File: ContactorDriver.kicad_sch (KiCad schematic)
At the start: 25 parts, among them J1 PowerConn, J2 DashboardConn, J3 ContactorConn, J4 FanConn1, J5 FanConn2, Q1 CSD18511KTT, Q3 CSD18511KTT, U1 RI3-1212S

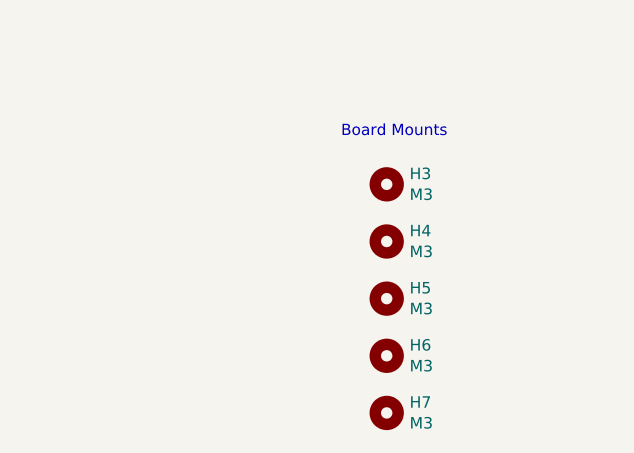
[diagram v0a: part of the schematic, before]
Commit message: Layout completed
Layout attempts to mirror connections on the original V2.1 CDB but in a drastically smaller package.
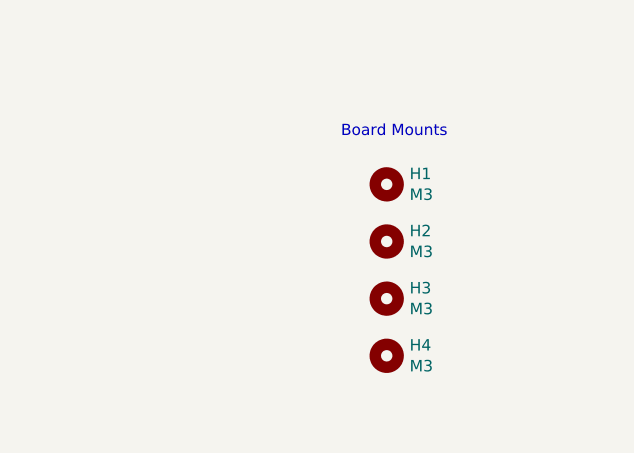
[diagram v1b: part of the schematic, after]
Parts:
- removed H7: M3, MountingHole:MountingHole_3mm, symbol Mechanical:MountingHole
- renumbered H3 to H1, H4 to H2, H5 to H3, H6 to H4
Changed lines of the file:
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@@
 		(on_board yes)
 		(dnp no)
-		(property "Reference" "H3"
+		(property "Reference" "H1"
 			(at 278.13 135.3566 0)
 			(effects
@@
 			(project "ContactorDriver"
 				(path "/aaa5c8ef-bb12-4c4a-bd2b-ddbca3d09ae8"
-					(reference "H3")
+					(reference "H1")
 					(unit 1)
 				)
@@
 		(on_board yes)
 		(dnp no)
-		(property "Reference" "H4"
+		(property "Reference" "H2"
 			(at 278.13 141.7066 0)
 			(effects
@@
 			(project "ContactorDriver"
 				(path "/aaa5c8ef-bb12-4c4a-bd2b-ddbca3d09ae8"
-					(reference "H4")
+					(reference "H2")
 					(unit 1)
 				)
@@
 		(on_board yes)
 		(dnp no)
-		(property "Reference" "H5"
+		(property "Reference" "H3"
 			(at 278.13 148.0566 0)
 			(effects
@@
 			(project "ContactorDriver"
 				(path "/aaa5c8ef-bb12-4c4a-bd2b-ddbca3d09ae8"
-					(reference "H5")
+					(reference "H3")
 					(unit 1)
 				)
@@
 		(on_board yes)
 		(dnp no)
-		(property "Reference" "H6"
+		(property "Reference" "H4"
 			(at 278.13 154.4066 0)
 			(effects
@@
 			(project "ContactorDriver"
 				(path "/aaa5c8ef-bb12-4c4a-bd2b-ddbca3d09ae8"
-					(reference "H6")
+					(reference "H4")
 					(unit 1)
 				)
@@
 					(unit 1)
 				)
-			)
-		)
-	)
-	(symbol
-		(lib_id "Mechanical:MountingHole")
-		(at 275.59 161.925 0)
-		(unit 1)
-		(exclude_from_sim no)
-		(in_bom yes)
-		(on_board yes)
-		(dnp no)
-		(property "Reference" "H7"
-			(at 278.13 160.7566 0)
-			(effects
-				(font
-					(size 1.27 1.27)
-				)
-				(justify left)
-			)
-		)
-		(property "Value" "M3"
-			(at 278.13 163.068 0)
-			(effects
-				(font
-					(size 1.27 1.27)
-				)
-				(justify left)
-			)
-		)
-		(property "Footprint" "MountingHole:MountingHole_3mm"
-			(at 275.59 161.925 0)
-			(effects
-				(font
-					(size 1.27 1.27)
-				)
-				(hide yes)
-			)
-		)
-		(property "Datasheet" "~"
-			(at 275.59 161.925 0)
-			(effects
-				(font
-					(size 1.27 1.27)
-				)
-				(hide yes)
-			)
-		)
-		(property "Description" ""
-			(at 275.59 161.925 0)
-			(effects
-				(font
-					(size 1.27 1.27)
-				)
-				(hide yes)
-			)
-		)
-		(instances
-			(project "ContactorDriver"
-				(path "/aaa5c8ef-bb12-4c4a-bd2b-ddbca3d09ae8"
-					(reference "H7")
-					(unit 1)
-				)

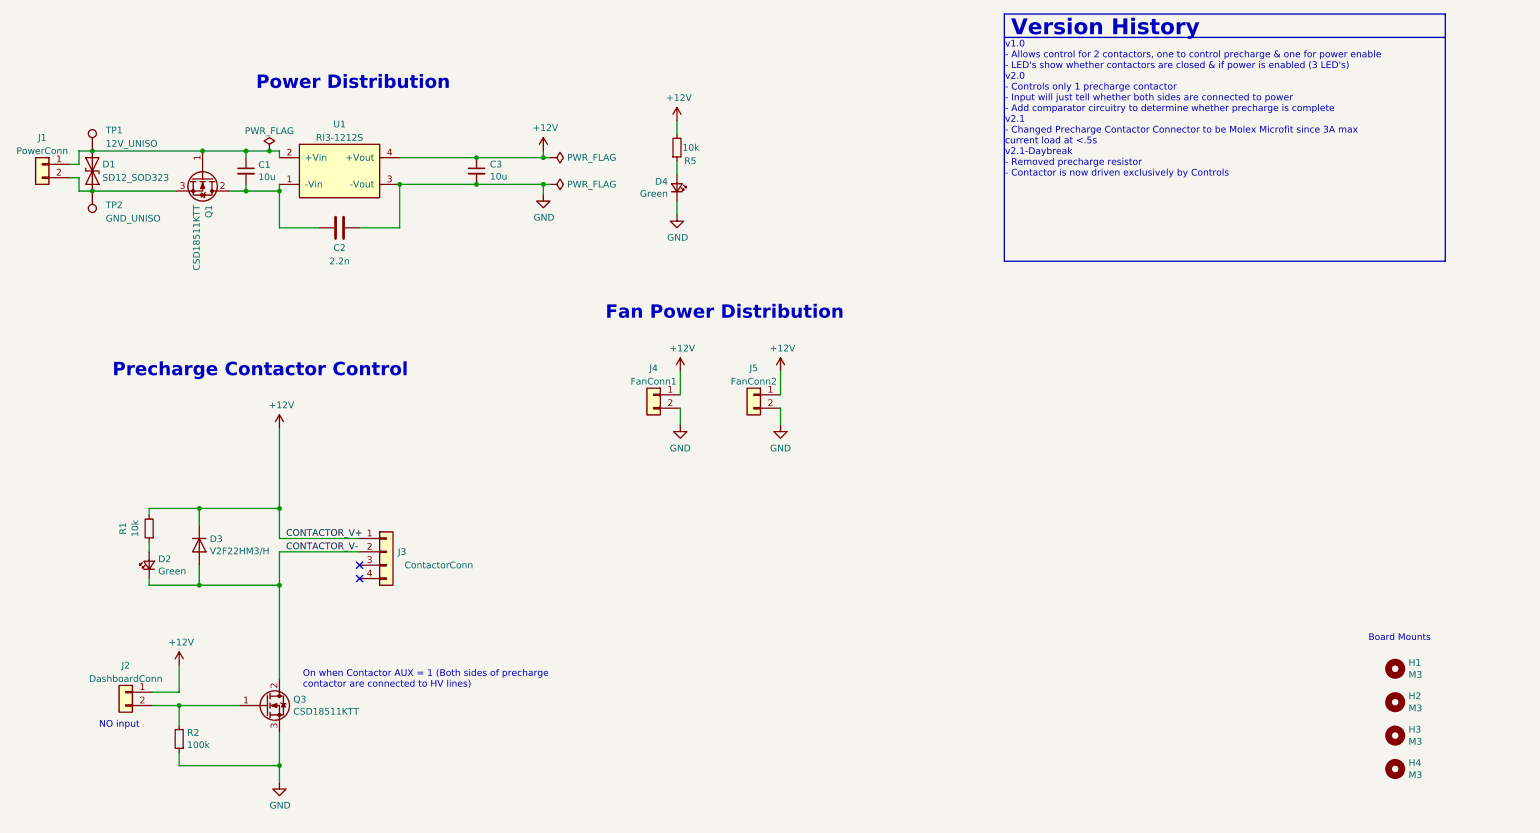
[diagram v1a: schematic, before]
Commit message: Updated Schematic
Updated Schematic to include ability to drive 2 contactors separately, and fans are now controlled by contactor signal as well.
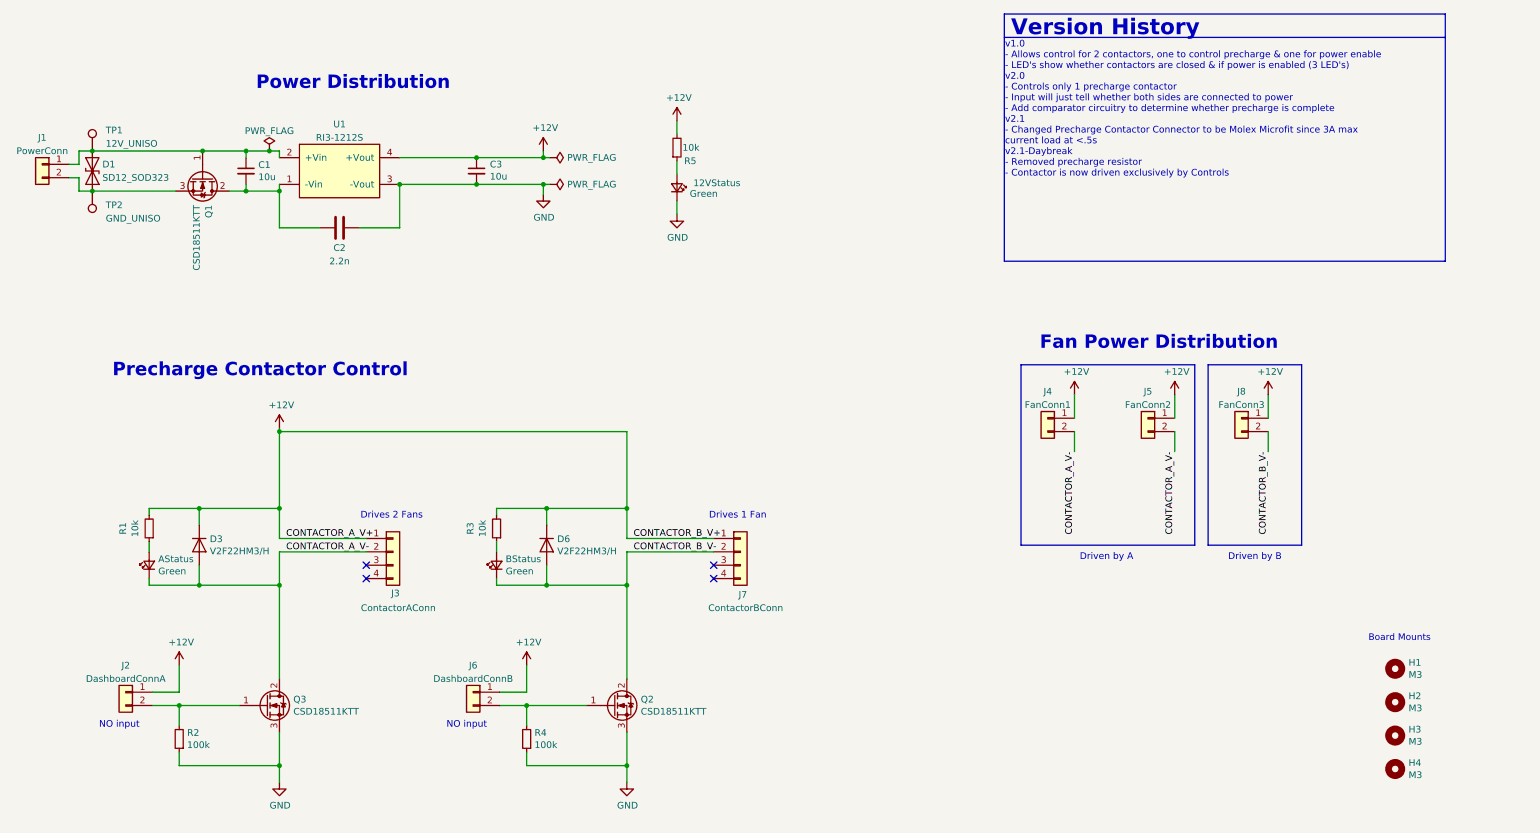
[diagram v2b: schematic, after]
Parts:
- added BStatus: Green, LED_SMD:LED_0805_2012Metric_Pad1.15x1.40mm_HandSolder, symbol Device:LED_Small
- added D6: V2F22HM3/H, UTSVT_Passive:V2F22HM, symbol Device:D
- added J6: DashboardConnB, Connector_Molex:Molex_Micro-Fit_3.0_43650-0200_1x02_P3.00mm_Horizontal, symbol Connector_Generic:Conn_01x02
- added J7: ContactorBConn, UTSVT_Connectors:Molex_MicroFit3.0_1x4xP3.00mm_PolarizingPeg_Vertical, symbol Connector_Generic:Conn_01x04
- added J8: FanConn3, Connector_Molex:Molex_Micro-Fit_3.0_43650-0200_1x02_P3.00mm_Horizontal, symbol Connector_Generic:Conn_01x02
- added Q2: CSD18511KTT, Package_TO_SOT_SMD:TO-252-2, symbol Device:Q_NMOS_GDS
- added R3: 10k, Resistor_SMD:R_0805_2012Metric, symbol Device:R_Small
- added R4: 100k, Resistor_SMD:R_0805_2012Metric_Pad1.20x1.40mm_HandSolder, symbol Device:R_Small
- J2: value DashboardConn -> DashboardConnA
- J3: value ContactorConn -> ContactorAConn
- renumbered D4 to 12VStatus, D2 to AStatus
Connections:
- net +12V: now also D6.1 (K), J6.1 (Pin_1), J7.1 (Pin_1), J8.1 (Pin_1), R3.2
- net GND: now also Q2.3 (S), R4.1; no longer J4.2 (Pin_2), J5.2 (Pin_2)
- net CONTACTOR_V- renamed CONTACTOR_A_V-
- net CONTACTOR_A_V-: now also J4.2 (Pin_2), J5.2 (Pin_2)
- new net: J6.2 (Pin_2), Q2.1 (G), R4.2
- new net: BStatus.2 (A), R3.1
- new net CONTACTOR_B_V-: BStatus.1 (K), D6.2 (A), J7.2 (Pin_2), J8.2 (Pin_2), Q2.2 (D)
- no-connect marks 2 -> 4
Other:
- note added: "Driven by A"
- note added: "Driven by B"
- note added: "Drives 1 Fan"
- note added: "Drives 2 Fans"
- note removed: "On when Contactor AUX = 1 (Both sides of precharge contactor are connected to HV lines)"
- moved on the sheet: J3, J4, J5

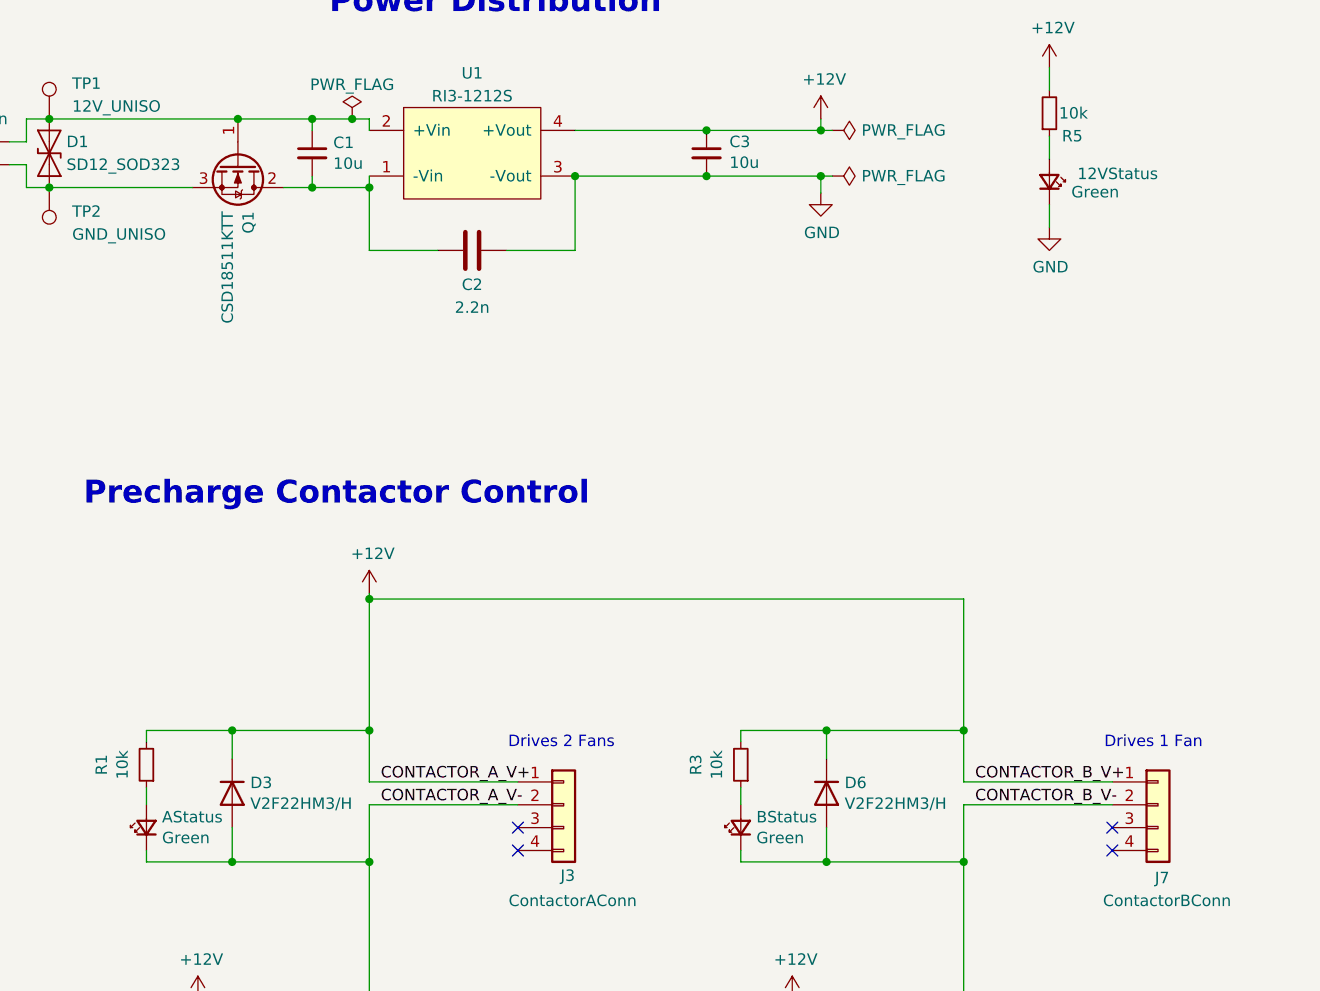
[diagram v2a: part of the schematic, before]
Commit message: Layout Updated
Updated layout to match updated schematic.
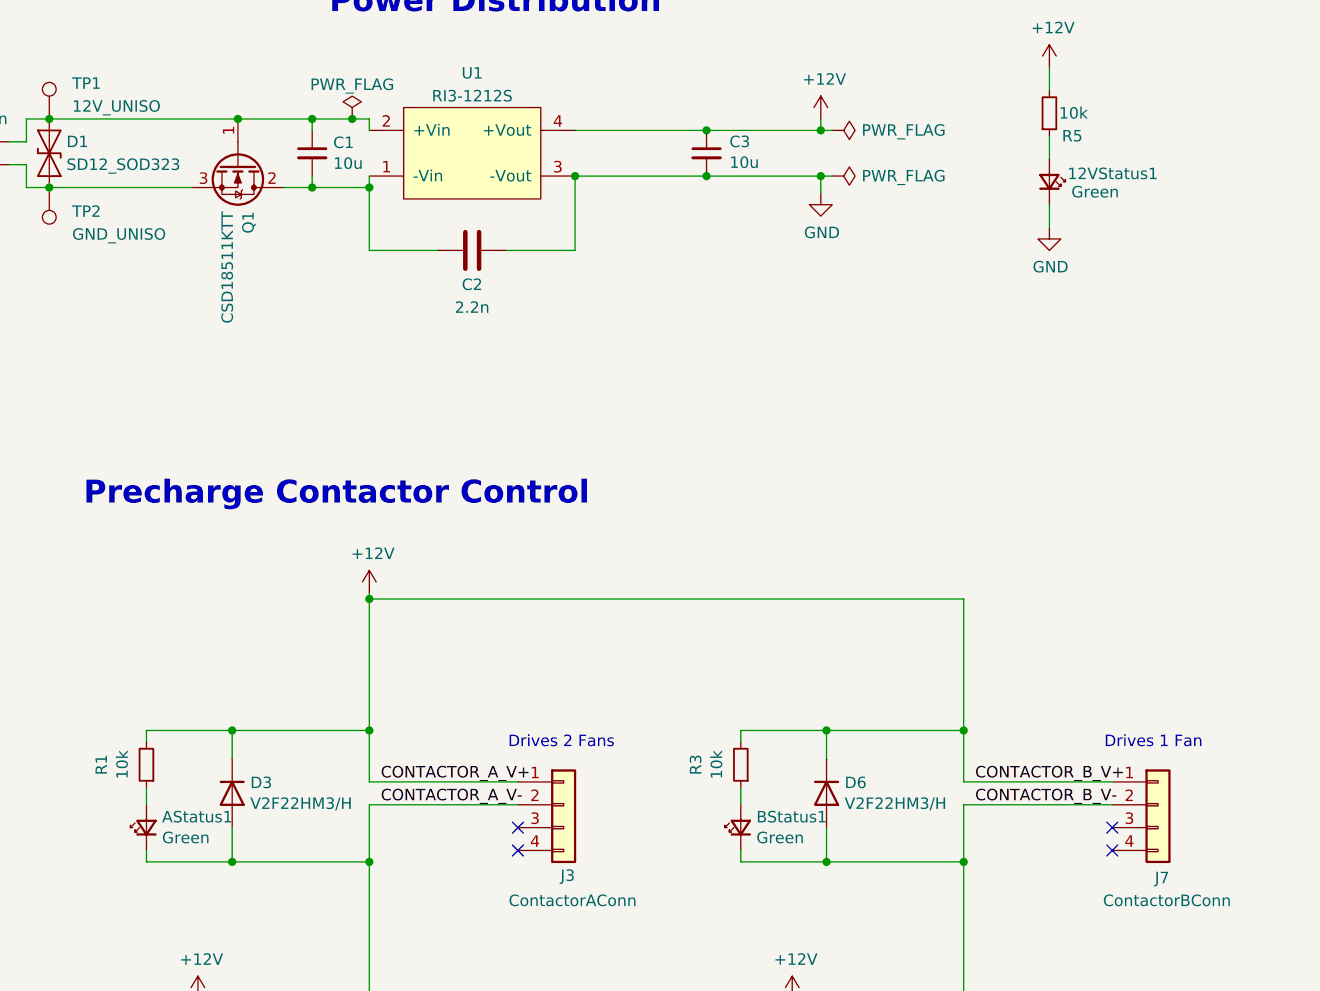
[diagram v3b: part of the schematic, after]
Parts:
- renumbered 12VStatus to 12VStatus1, AStatus to AStatus1, BStatus to BStatus1
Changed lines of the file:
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@@
 		(on_board yes)
 		(dnp no)
-		(property "Reference" "AStatus"
+		(property "Reference" "AStatus1"
 			(at 40.4622 115.6716 90)
 			(effects
@@
 			(project "ContactorDriver"
 				(path "/aaa5c8ef-bb12-4c4a-bd2b-ddbca3d09ae8"
-					(reference "AStatus")
+					(reference "AStatus1")
 					(unit 1)
 				)
@@
 		(on_board yes)
 		(dnp no)
-		(property "Reference" "12VStatus"
+		(property "Reference" "12VStatus1"
 			(at 151.13 44.196 90)
 			(effects
@@
 			(project "ContactorDriver"
 				(path "/aaa5c8ef-bb12-4c4a-bd2b-ddbca3d09ae8"
-					(reference "12VStatus")
+					(reference "12VStatus1")
 					(unit 1)
 				)
@@
 		(on_board yes)
 		(dnp no)
-		(property "Reference" "BStatus"
+		(property "Reference" "BStatus1"
 			(at 106.5022 115.6716 90)
 			(effects
@@
 			(project "ContactorDriver"
 				(path "/aaa5c8ef-bb12-4c4a-bd2b-ddbca3d09ae8"
-					(reference "BStatus")
+					(reference "BStatus1")
 					(unit 1)
 				)

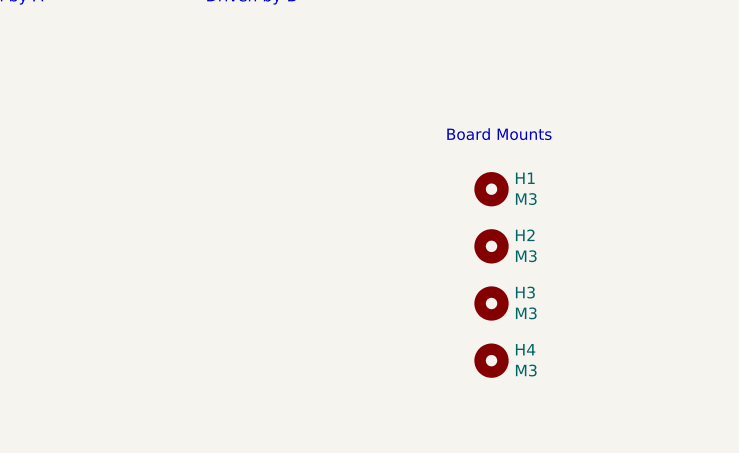
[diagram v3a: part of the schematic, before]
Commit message: Added images
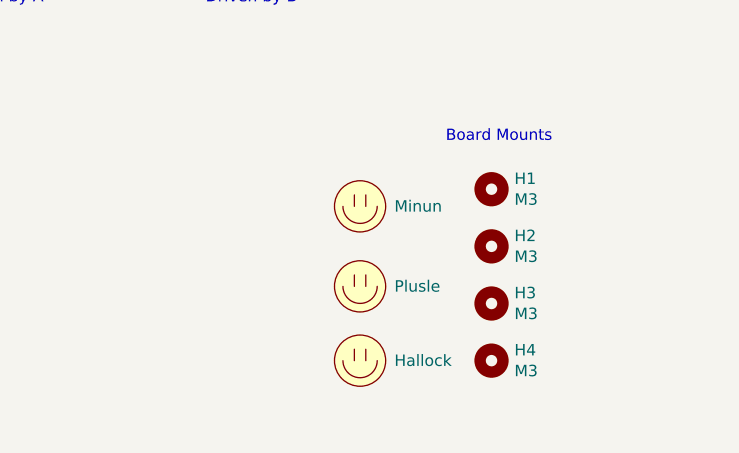
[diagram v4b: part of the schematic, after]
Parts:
- added LOGO1: Hallock, UTSVT_Special:Hallock_Image_Tiny, symbol utsvt-misc:Logo_Placeholder
- added LOGO2: Plusle, Board:plusle, symbol utsvt-misc:Logo_Placeholder
- added LOGO3: Minun, Board:minun, symbol utsvt-misc:Logo_Placeholder
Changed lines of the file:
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@@
+	)
+	(symbol
+		(lib_id "utsvt-misc:Logo_Placeholder")
+		(at 260.985 147.32 0)
+		(unit 1)
+		(exclude_from_sim no)
+		(in_bom yes)
+		(on_board yes)
+		(dnp no)
+		(fields_autoplaced yes)
+		(property "Reference" "LOGO2"
+			(at 260.985 143.51 0)
+			(effects
+				(font
+					(size 1.27 1.27)
+				)
+				(hide yes)
+			)
+		)
+		(property "Value" "Plusle"
+			(at 264.795 147.3199 0)
+			(effects
+				(font
+					(size 1.27 1.27)
+				)
+				(justify left)
+			)
+		)
+		(property "Footprint" "Board:plusle"
+			(at 260.985 145.415 0)
+			(effects
+				(font
+					(size 1.27 1.27)
+				)
+				(hide yes)
+			)
+		)
+		(property "Datasheet" ""
+			(at 260.985 145.415 0)
+			(effects
+				(font
+					(size 1.27 1.27)
+				)
+				(hide yes)
+			)
+		)
+		(property "Description" "Graph footprint placeholder"
+			(at 260.985 147.32 0)
+			(effects
+				(font
+					(size 1.27 1.27)
+				)
+				(hide yes)
+			)
+		)
+		(instances
+			(project "ContactorDriver"
+				(path "/aaa5c8ef-bb12-4c4a-bd2b-ddbca3d09ae8"
+					(reference "LOGO2")
+					(unit 1)
+				)
+			)
+		)
+	)
+	(symbol
+		(lib_id "utsvt-misc:Logo_Placeholder")
+		(at 260.985 155.575 0)
+		(unit 1)
+		(exclude_from_sim no)
+		(in_bom yes)
+		(on_board yes)
+		(dnp no)
+		(fields_autoplaced yes)
+		(property "Reference" "LOGO1"
+			(at 260.985 151.765 0)
+			(effects
+				(font
+					(size 1.27 1.27)
+				)
+				(hide yes)
+			)
+		)
+		(property "Value" "Hallock"
+			(at 264.795 155.5749 0)
+			(effects
+				(font
+					(size 1.27 1.27)
+				)
+				(justify left)
+			)
+		)
+		(property "Footprint" "UTSVT_Special:Hallock_Image_Tiny"
+			(at 260.985 153.67 0)
+			(effects
+				(font
+					(size 1.27 1.27)
+				)
+				(hide yes)
+			)
+		)
+		(property "Datasheet" ""
+			(at 260.985 153.67 0)
+			(effects
+				(font
+					(size 1.27 1.27)
+				)
+				(hide yes)
+			)
+		)
+		(property "Description" "Graph footprint placeholder"
+			(at 260.985 155.575 0)
+			(effects
+				(font
+					(size 1.27 1.27)
+				)
+				(hide yes)
+			)
+		)
+		(instances
+			(project "ContactorDriver"
+				(path "/aaa5c8ef-bb12-4c4a-bd2b-ddbca3d09ae8"
+					(reference "LOGO1")
+					(unit 1)
+				)
+			)
+		)
 	)
 	(symbol
@@
 					(unit 1)
 				)
+			)
+		)
+	)
+	(symbol
+		(lib_id "utsvt-misc:Logo_Placeholder")
+		(at 260.985 138.43 0)
+		(unit 1)
+		(exclude_from_sim no)
+		(in_bom yes)
+		(on_board yes)
+		(dnp no)
+		(fields_autoplaced yes)
+		(property "Reference" "LOGO3"
+			(at 260.985 134.62 0)
+			(effects
+				(font
+					(size 1.27 1.27)
+				)
+				(hide yes)
+			)
+		)
+		(property "Value" "Minun"
+			(at 264.795 138.4299 0)
+			(effects
+				(font
+					(size 1.27 1.27)
+				)
+				(justify left)
+			)
+		)
+		(property "Footprint" "Board:minun"
+			(at 260.985 136.525 0)
+			(effects
+				(font
+					(size 1.27 1.27)
+				)
+				(hide yes)
+			)
+		)
+		(property "Datasheet" ""
+			(at 260.985 136.525 0)
+			(effects
+				(font
+					(size 1.27 1.27)
+				)
+				(hide yes)
+			)
+		)
+		(property "Description" "Graph footprint placeholder"
+			(at 260.985 138.43 0)
+			(effects
+				(font
+					(size 1.27 1.27)
+				)
+				(hide yes)
+			)
+		)
+		(instances
+			(project "ContactorDriver"
+				(path "/aaa5c8ef-bb12-4c4a-bd2b-ddbca3d09ae8"
+					(reference "LOGO3")
+					(unit 1)
+				)
